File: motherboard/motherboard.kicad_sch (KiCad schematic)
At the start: 56 parts, among them J1 SL-10 (L-KLS1-603C-10-S), J10 SL-10 (L-KLS1-603C-10-S), J11 SL-10 (L-KLS1-603C-10-S), J12 SL-10 (L-KLS1-603C-10-S), J13 SL-10 (L-KLS1-603C-10-S), J14 SL-10 (L-KLS1-603C-10-S), J15 SL-10 (L-KLS1-603C-10-S), J16 SL-10 (L-KLS1-603C-10-S), J17 SL-10 (L-KLS1-603C-10-S), J18 SL-10 (L-KLS1-603C-10-S)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

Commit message: DC, contr, mb, step v2
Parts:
- added J28: PinHeader_1x02_P2.54mm (Contr +24V), Connector_PinHeader_2.54mm:PinHeader_1x02_P2.54mm_Vertical, symbol Connector:Conn_01x02_Pin
- added J29: PinHeader_1x04_P2.54mm (RS485), Connector_PinHeader_2.54mm:PinHeader_1x04_P2.54mm_Vertical, symbol Connector:Conn_01x04_Pin
- added J30: PinHeader_2x07_P2.54mm (RTS), Connector_PinHeader_2.54mm:PinHeader_2x07_P2.54mm_Vertical, symbol Connector_Generic:Conn_02x07_Odd_Even
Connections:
- net +24V: now also J28.2 (Pin_2)
- net +3.3VRS485: now also J29.1 (Pin_1)
- net A: now also J29.3 (Pin_3)
- net B: now also J29.4 (Pin_4)
- net GND1: now also J29.2 (Pin_2), J30.13 (Pin_13), J30.14 (Pin_14)
- net GNDA: now also J28.1 (Pin_1)
- net RTS1: now also J30.1 (Pin_1)
- net RTS10: now also J30.10 (Pin_10)
- net RTS11: now also J30.11 (Pin_11)
- net RTS12: now also J30.12 (Pin_12)
- net RTS2: now also J30.2 (Pin_2)
- net RTS3: now also J30.3 (Pin_3)
- net RTS4: now also J30.4 (Pin_4)
- net RTS5: now also J30.5 (Pin_5)
- net RTS6: now also J30.6 (Pin_6)
- net RTS7: now also J30.7 (Pin_7)
- net RTS8: now also J30.8 (Pin_8)
- net RTS9: now also J30.9 (Pin_9)

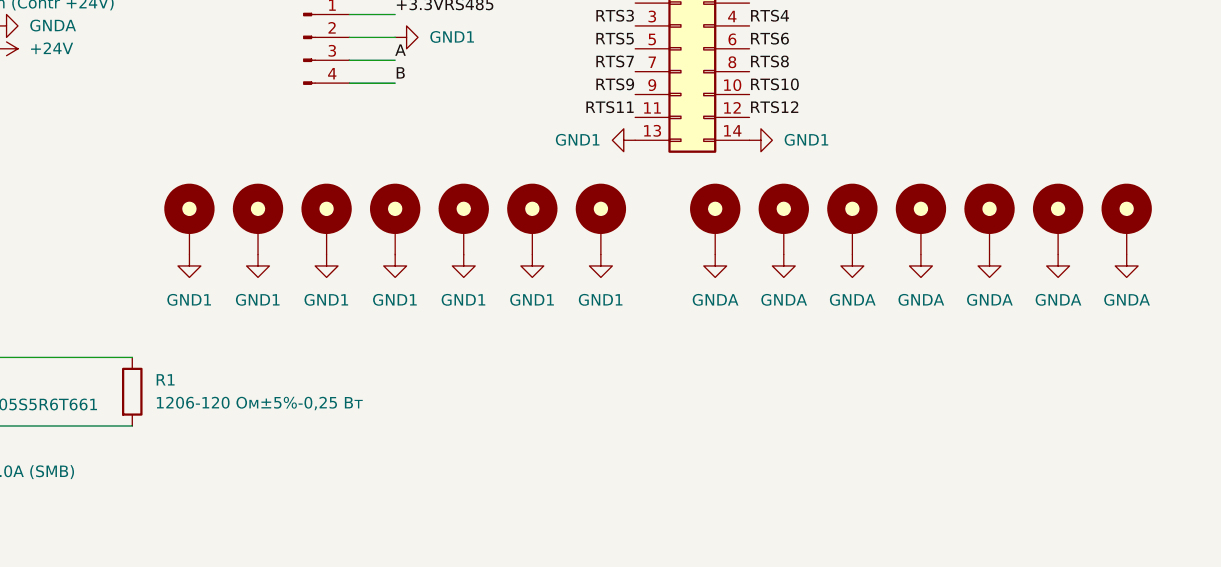
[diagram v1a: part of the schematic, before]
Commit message: DC, contr, mb, digit in v2.1
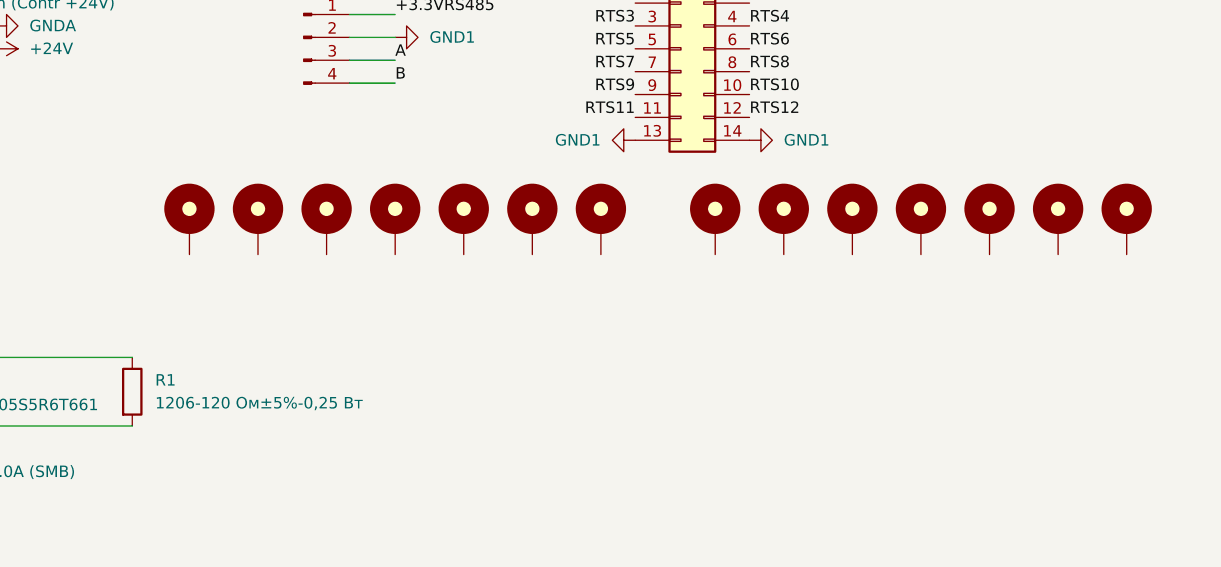
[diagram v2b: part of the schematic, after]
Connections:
- net GND1: no longer H1.1, H13.1, H2.1, H3.1, H4.1, H5.1, H6.1
- net GNDA: no longer H10.1, H11.1, H12.1, H14.1, H7.1, H8.1, H9.1

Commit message: motherboard установлены тестовые площадки
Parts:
- added TP1, TP10, TP11, TP12, TP13, TP14, TP15, TP16, TP17, TP2, TP3, TP4, TP5, TP6, TP7, TP8, TP9: TestPoint, PCM_4ms_TestPoint:TestPoint_D1, symbol Connector:TestPoint
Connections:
- net +24V: now also TP16.1
- net +3.3VRS485: now also TP15.1
- net A: now also TP1.1
- net B: now also TP2.1
- net GND1: now also TP17.1
- net GNDA: now also TP14.1
- net RTS1: now also TP3.1
- net RTS10: now also TP13.1
- net RTS11: now also TP8.1
- net RTS2: now also TP9.1
- net RTS3: now also TP4.1
- net RTS4: now also TP10.1
- net RTS5: now also TP5.1
- net RTS6: now also TP11.1
- net RTS7: now also TP6.1
- net RTS8: now also TP12.1
- net RTS9: now also TP7.1
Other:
- moved on the sheet: J1, J10, J11, J2, J3, J4, J5, J6, J7, J8, J9, L2

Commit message: mother board refresh
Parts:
- D1, D10, D2, D3, D4, D5, D6, D7, D8, D9: footprint PCM_Diode_SMD_AKL:D_SMB -> Diode_SMD:D_SMB
- H1, H10, H11, H12, H13, H14, H2, H3, H4, H5, H6, H7, H8, H9: footprint PCM_SL_Mechanical:MountingHole_3.2mm_Pad -> MountingHole:MountingHole_3.2mm_M3
- R1: footprint PCM_Resistor_SMD_AKL:R_1206_3216Metric -> Resistor_SMD:R_1206_3216Metric
- RV1, RV2, RV3, RV4, RV5: footprint PCM_4ms_Resistor:R_0805_2012Metric -> Resistor_SMD:R_0805_2012Metric
- TP1, TP17, TP2: footprint PCM_4ms_TestPoint:TestPoint_D1 -> TestPoint:TestPoint_Pad_D1.0mm
- TP10, TP11, TP12, TP13, TP4, TP5, TP6, TP7, TP8, TP9: now left out of the parts list
- TP3: footprint PCM_4ms_TestPoint:TestPoint_D1 -> TestPoint:TestPoint_Pad_D1.0mm; now left out of the parts list

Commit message: update schemas
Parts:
- TP1, TP14, TP15, TP16, TP17, TP2: now left out of the parts list
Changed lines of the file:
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@@
 		(unit 1)
 		(exclude_from_sim no)
-		(in_bom yes)
+		(in_bom no)
 		(on_board yes)
 		(dnp no)
@@
 					(size 1.27 1.27)
 				)
+				(hide yes)
 			)
 		)
@@
 		(unit 1)
 		(exclude_from_sim no)
-		(in_bom yes)
+		(in_bom no)
 		(on_board yes)
 		(dnp no)
@@
 				)
 				(justify left)
+				(hide yes)
 			)
 		)
@@
 		(unit 1)
 		(exclude_from_sim no)
-		(in_bom yes)
+		(in_bom no)
 		(on_board yes)
 		(dnp no)
@@
 					(size 1.27 1.27)
 				)
+				(hide yes)
 			)
 		)
@@
 		(unit 1)
 		(exclude_from_sim no)
-		(in_bom yes)
+		(in_bom no)
 		(on_board yes)
 		(dnp no)
@@
 					(size 1.27 1.27)
 				)
+				(hide yes)
 			)
 		)
@@
 		(unit 1)
 		(exclude_from_sim no)
-		(in_bom yes)
+		(in_bom no)
 		(on_board yes)
 		(dnp no)
@@
 					(size 1.27 1.27)
 				)
+				(hide yes)
 			)
 		)
@@
 		(unit 1)
 		(exclude_from_sim no)
-		(in_bom yes)
+		(in_bom no)
 		(on_board yes)
 		(dnp no)
@@
 				)
 				(justify left)
+				(hide yes)
 			)
 		)
